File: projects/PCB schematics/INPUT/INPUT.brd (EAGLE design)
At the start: 160 x 100 mm, 84 parts, among them IC1 OP11D, IC10 74AHC1G32DCK, IC13 OP11D, IC14 74AHC1G32DCK, IC17 OP11D, IC18 74AHC1G32DCK, IC19 OP11D, IC20 OP11D, IC3 OP11D, IC4 OP11D, IC5 OP11D, IC6 74AHC1G32DCK, IC7 OP11D, IC8 OP11D, IC9 74AHC1G32DCK

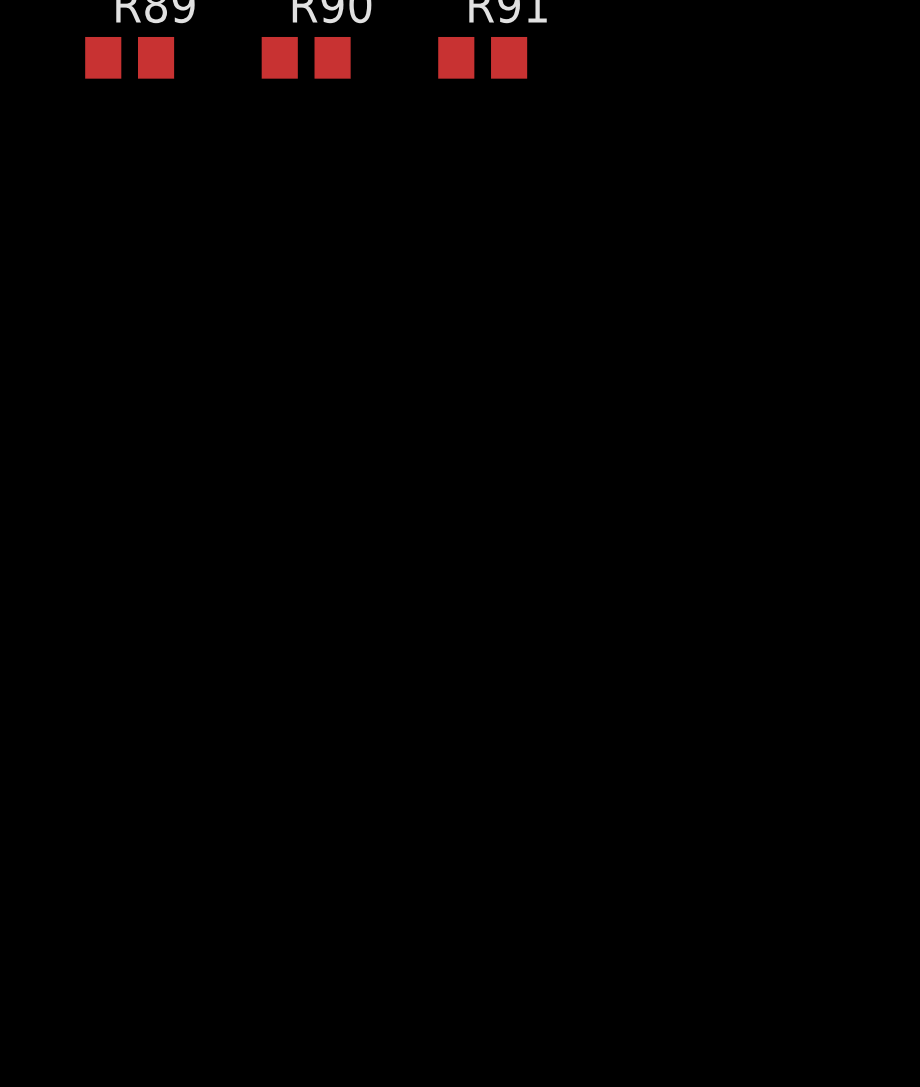
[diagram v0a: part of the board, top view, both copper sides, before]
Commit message: BSPD - Schematic revision/component revision.
During ESF, schematics chosen used European part libraries.
These were updated to US symbols, with appropriate final parts sourced
to allow builds of both SOP8 and DIL-8 packages.
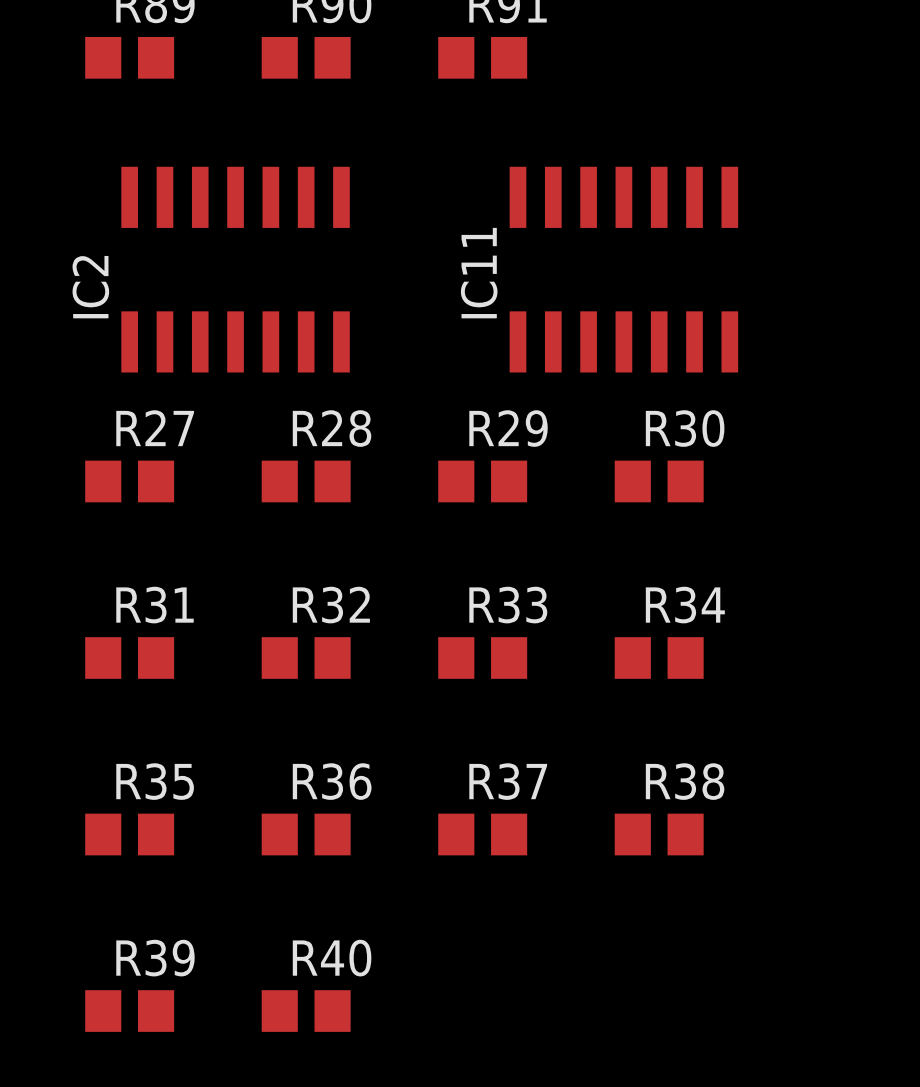
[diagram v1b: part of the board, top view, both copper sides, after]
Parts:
- added IC11, IC2: OP11D, linear:SO14
- added R27, R34: 12k, rcl:R0805
- added R28, R35: 27k, rcl:R0805
- added R29, R30, R31, R32, R33, R36, R37, R38, R39, R40: 1k, rcl:R0805
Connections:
- new net BSE_INPUT: R27.2
- new net BSE_PROCESSED: IC2.1
- new net MOTCUR_INPUT: R34.2
- new net MOTCUR_PROCESSED: IC11.1
- new net N$19: IC2.3, R31.1, R32.2
- new net N$21: R27.1, R28.2, R29.2
- new net N$22: R32.1, R33.1
- new net N$25: IC2.2, R29.1, R30.1
- new net N$32: IC11.3, R38.1, R39.2
- new net N$33: R34.1, R35.2, R36.2
- new net N$36: R39.1, R40.1
- new net N$37: IC11.2, R36.1, R37.1
- net +1.0V: now also R30.2, R37.2
- net GND: now also R28.1, R31.2, R33.2, R35.1, R38.2, R40.2
- net V+: now also IC11.4, IC2.4
- net V-: now also IC11.11, IC2.11
